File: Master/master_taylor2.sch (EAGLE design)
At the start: 43 parts, among them J1 ISP, U1 ATMEGA128RFA1, U2 TPS73633-DBVT, U3 ULN2003ADR, Y1 16MHz

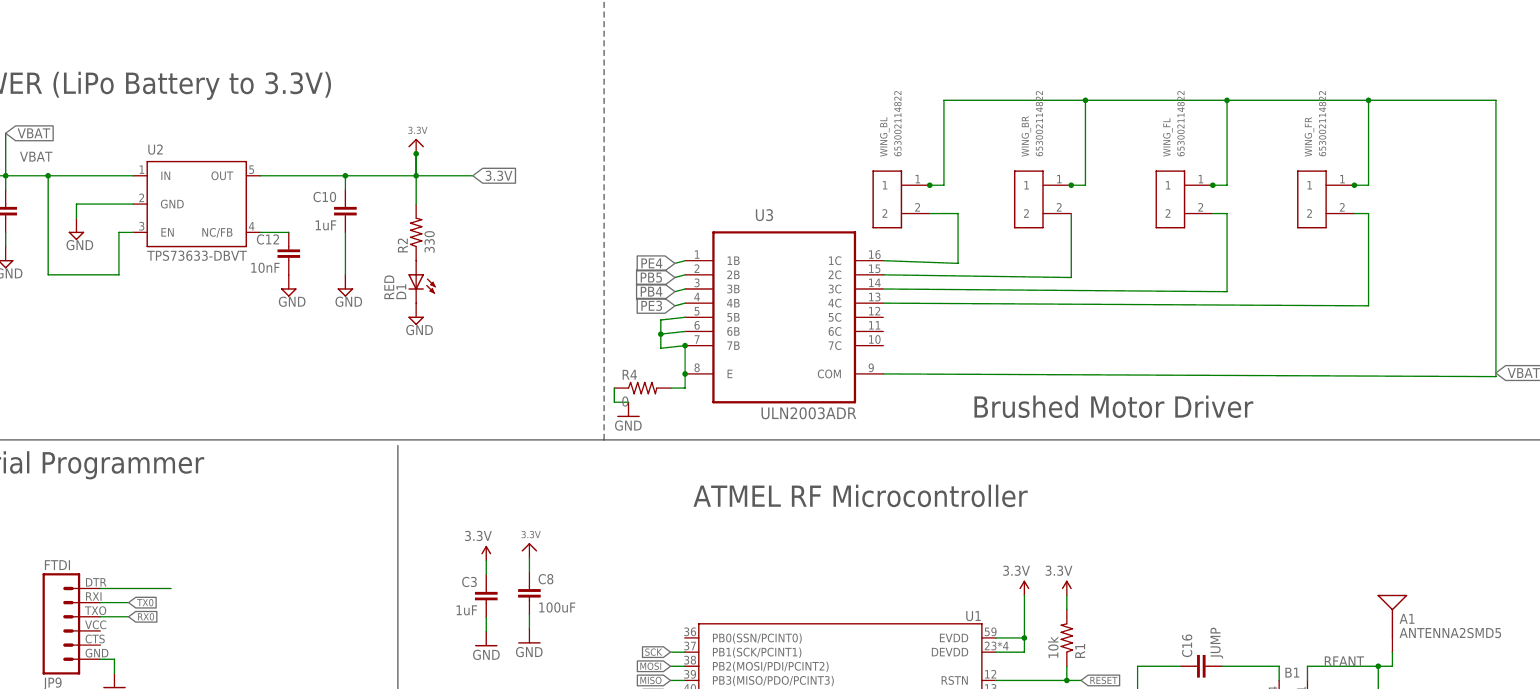
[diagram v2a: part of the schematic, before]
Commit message: Added caps near each motor
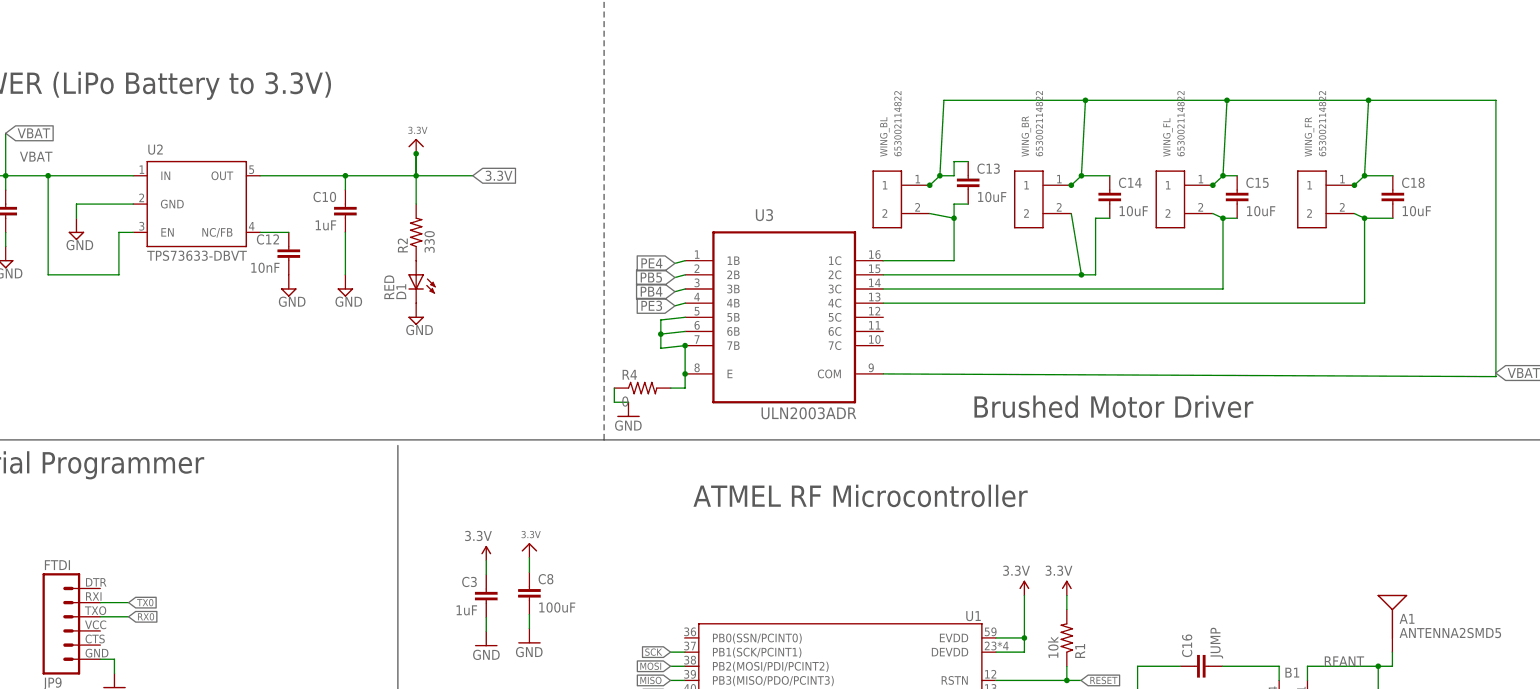
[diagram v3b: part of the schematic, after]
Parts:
- added C13, C14, C15, C18: 10uF, SparkFun-Capacitors:CAP0603-CAP
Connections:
- removed net DTR: JP9.1
- net N$29: now also C13.2
- net N$30: now also C14.2
- net N$31: now also C15.2
- net N$32: now also C18.2
- net VBAT: now also C13.1, C14.1, C15.1, C18.1
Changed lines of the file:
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@@
 <setting verticaltext="up"/>
 </settings>
-<grid distance="0.1" unitdist="inch" unit="inch" style="lines" multiple="1" display="no" altdistance="0.01" altunitdist="inch" altunit="inch"/>
+<grid distance="0.1" unitdist="inch" unit="inch" style="lines" multiple="1" display="yes" altdistance="0.01" altunitdist="inch" altunit="inch"/>
 <layers>
 <layer number="1" name="Top" color="4" fill="1" visible="no" active="no"/>
@@
 <part name="U$8" library="microbuilder" deviceset="3.3V" device=""/>
 <part name="GND8" library="SparkFun-Aesthetics" deviceset="GND" device=""/>
+<part name="C13" library="SparkFun-Capacitors" deviceset="CAP" device="0603-CAP" value="10uF"/>
+<part name="C14" library="SparkFun-Capacitors" deviceset="CAP" device="0603-CAP" value="10uF"/>
+<part name="C15" library="SparkFun-Capacitors" deviceset="CAP" device="0603-CAP" value="10uF"/>
+<part name="C18" library="SparkFun-Capacitors" deviceset="CAP" device="0603-CAP" value="10uF"/>
 </parts>
 <sheets>
@@
 <instance part="U$8" gate="G$1" x="-152.4" y="213.36"/>
 <instance part="GND8" gate="1" x="-152.4" y="195.58"/>
+<instance part="C13" gate="G$1" x="-73.66" y="276.86"/>
+<instance part="C14" gate="G$1" x="-48.26" y="274.32"/>
+<instance part="C15" gate="G$1" x="-25.4" y="274.32"/>
+<instance part="C18" gate="G$1" x="2.54" y="274.32"/>
 </instances>
 <busses>
@@
 </segment>
 </net>
-<net name="DTR" class="0">
-<segment>
-<pinref part="JP9" gate="G$1" pin="1"/>
-<wire x1="-216.7" y1="205.34" x2="-229.4" y2="205.34" width="0.1524" layer="91"/>
-</segment>
-</net>
 <net name="N$7" class="0">
 <segment>
@@
 <segment>
 <pinref part="U3" gate="A" pin="1C"/>
-<wire x1="-88.9" y1="264.16" x2="-75.48" y2="263.68" width="0.1524" layer="91"/>
-<wire x1="-75.48" y1="263.68" x2="-75.48" y2="272.62" width="0.1524" layer="91"/>
+<wire x1="-88.9" y1="264.16" x2="-76.2" y2="264.16" width="0.1524" layer="91"/>
+<wire x1="-76.2" y1="264.16" x2="-76.2" y2="271.78" width="0.1524" layer="91"/>
 <pinref part="WING_BL" gate="G$1" pin="2"/>
-<wire x1="-75.48" y1="272.62" x2="-80.56" y2="272.62" width="0.1524" layer="91"/>
+<wire x1="-76.2" y1="271.78" x2="-80.56" y2="272.62" width="0.1524" layer="91"/>
+<wire x1="-73.66" y1="274.32" x2="-76.2" y2="274.32" width="0.1524" layer="91"/>
+<wire x1="-76.2" y1="274.32" x2="-76.2" y2="271.78" width="0.1524" layer="91"/>
+<junction x="-76.2" y="271.78"/>
+<pinref part="C13" gate="G$1" pin="2"/>
 </segment>
 </net>
@@
 <pinref part="U3" gate="A" pin="2C"/>
 <pinref part="WING_BR" gate="G$1" pin="2"/>
-<wire x1="-88.9" y1="261.62" x2="-55.16" y2="261.14" width="0.1524" layer="91"/>
-<wire x1="-55.16" y1="261.14" x2="-55.16" y2="272.62" width="0.1524" layer="91"/>
+<wire x1="-88.9" y1="261.62" x2="-53.34" y2="261.62" width="0.1524" layer="91"/>
+<wire x1="-53.34" y1="261.62" x2="-55.16" y2="272.62" width="0.1524" layer="91"/>
+<wire x1="-48.26" y1="271.78" x2="-50.8" y2="271.78" width="0.1524" layer="91"/>
+<wire x1="-50.8" y1="271.78" x2="-50.8" y2="261.62" width="0.1524" layer="91"/>
+<wire x1="-50.8" y1="261.62" x2="-53.34" y2="261.62" width="0.1524" layer="91"/>
+<junction x="-53.34" y="261.62"/>
+<pinref part="C14" gate="G$1" pin="2"/>
 </segment>
 </net>
@@
 <segment>
 <pinref part="U3" gate="A" pin="3C"/>
-<wire x1="-88.9" y1="259.08" x2="-27.22" y2="258.6" width="0.1524" layer="91"/>
-<wire x1="-27.22" y1="258.6" x2="-27.22" y2="272.62" width="0.1524" layer="91"/>
+<wire x1="-88.9" y1="259.08" x2="-27.94" y2="259.08" width="0.1524" layer="91"/>
+<wire x1="-27.94" y1="259.08" x2="-27.94" y2="271.78" width="0.1524" layer="91"/>
 <pinref part="WING_FL" gate="G$1" pin="2"/>
-<wire x1="-27.22" y1="272.62" x2="-29.76" y2="272.62" width="0.1524" layer="91"/>
+<wire x1="-27.94" y1="271.78" x2="-29.76" y2="272.62" width="0.1524" layer="91"/>
+<wire x1="-27.94" y1="271.78" x2="-25.4" y2="271.78" width="0.1524" layer="91"/>
+<junction x="-27.94" y="271.78"/>
+<pinref part="C15" gate="G$1" pin="2"/>
 </segment>
 </net>
@@
 <segment>
 <pinref part="U3" gate="A" pin="4C"/>
-<wire x1="-88.9" y1="256.54" x2="-1.82" y2="256.06" width="0.1524" layer="91"/>
-<wire x1="-1.82" y1="256.06" x2="-1.82" y2="272.62" width="0.1524" layer="91"/>
+<wire x1="-88.9" y1="256.54" x2="-2.54" y2="256.54" width="0.1524" layer="91"/>
+<wire x1="-2.54" y1="256.54" x2="-2.54" y2="271.78" width="0.1524" layer="91"/>
 <pinref part="WING_FR" gate="G$1" pin="2"/>
-<wire x1="-1.82" y1="272.62" x2="-4.36" y2="272.62" width="0.1524" layer="91"/>
+<wire x1="-2.54" y1="271.78" x2="-4.36" y2="272.62" width="0.1524" layer="91"/>
+<wire x1="-2.54" y1="271.78" x2="2.54" y2="271.78" width="0.1524" layer="91"/>
+<junction x="-2.54" y="271.78"/>
+<pinref part="C18" gate="G$1" pin="2"/>
 </segment>
 </net>
@@
 <wire x1="-27.22" y1="292.94" x2="-52.62" y2="292.94" width="0.1524" layer="91"/>
 <wire x1="-52.62" y1="292.94" x2="-78.02" y2="292.94" width="0.1524" layer="91"/>
-<wire x1="-78.02" y1="292.94" x2="-78.02" y2="277.7" width="0.1524" layer="91"/>
+<wire x1="-78.02" y1="292.94" x2="-78.74" y2="279.4" width="0.1524" layer="91"/>
 <pinref part="WING_BL" gate="G$1" pin="1"/>
-<wire x1="-78.02" y1="277.7" x2="-80.56" y2="277.7" width="0.1524" layer="91"/>
+<wire x1="-78.74" y1="279.4" x2="-80.56" y2="277.7" width="0.1524" layer="91"/>
 <pinref part="WING_BR" gate="G$1" pin="1"/>
-<wire x1="-55.16" y1="277.7" x2="-52.62" y2="277.7" width="0.1524" layer="91"/>
-<wire x1="-52.62" y1="277.7" x2="-52.62" y2="292.94" width="0.1524" layer="91"/>
+<wire x1="-55.16" y1="277.7" x2="-53.34" y2="279.4" width="0.1524" layer="91"/>
+<wire x1="-53.34" y1="279.4" x2="-52.62" y2="292.94" width="0.1524" layer="91"/>
 <pinref part="WING_FL" gate="G$1" pin="1"/>
-<wire x1="-29.76" y1="277.7" x2="-27.22" y2="277.7" width="0.1524" layer="91"/>
-<wire x1="-27.22" y1="277.7" x2="-27.22" y2="292.94" width="0.1524" layer="91"/>
-<wire x1="-1.82" y1="277.7" x2="-1.82" y2="292.94" width="0.1524" layer="91"/>
+<wire x1="-29.76" y1="277.7" x2="-27.94" y2="279.4" width="0.1524" layer="91"/>
+<wire x1="-27.94" y1="279.4" x2="-27.22" y2="292.94" width="0.1524" layer="91"/>
+<wire x1="-2.54" y1="279.4" x2="-1.82" y2="292.94" width="0.1524" layer="91"/>
 <pinref part="WING_FR" gate="G$1" pin="1"/>
-<wire x1="-4.36" y1="277.7" x2="-1.82" y2="277.7" width="0.1524" layer="91"/>
+<wire x1="-4.36" y1="277.7" x2="-2.54" y2="279.4" width="0.1524" layer="91"/>
 <junction x="-27.22" y="292.94"/>
 <junction x="-52.62" y="292.94"/>
@@
 <junction x="-4.36" y="277.7"/>
 <label x="21" y="244" size="1.778" layer="97" xref="yes"/>
-</segment>
-</net>
+<wire x1="-78.74" y1="279.4" x2="-76.2" y2="279.4" width="0.1524" layer="91"/>
+<wire x1="-76.2" y1="279.4" x2="-76.2" y2="281.94" width="0.1524" layer="91"/>
+<wire x1="-76.2" y1="281.94" x2="-73.66" y2="281.94" width="0.1524" layer="91"/>
+<wire x1="-27.94" y1="279.4" x2="-25.4" y2="279.4" width="0.1524" layer="91"/>
+<wire x1="-2.54" y1="279.4" x2="2.54" y2="279.4" width="0.1524" layer="91"/>
+<wire x1="-53.34" y1="279.4" x2="-48.26" y2="279.4" width="0.1524" layer="91"/>
+<junction x="-53.34" y="279.4"/>
+<junction x="-27.94" y="279.4"/>
+<junction x="-2.54" y="279.4"/>
+<junction x="-78.74" y="279.4"/>
+<pinref part="C13" gate="G$1" pin="1"/>
+<pinref part="C14" gate="G$1" pin="1"/>
+<pinref part="C15" gate="G$1" pin="1"/>
+<pinref part="C18" gate="G$1" pin="1"/>
+</segment>
+</net>

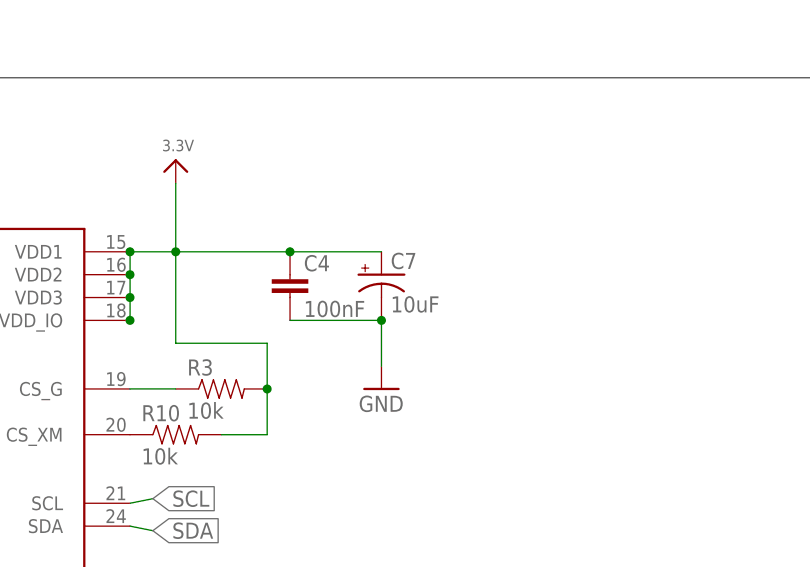
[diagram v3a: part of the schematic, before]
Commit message: Sparkfun's electrolytic footprint seemed sketchy so I switched to microbuilder
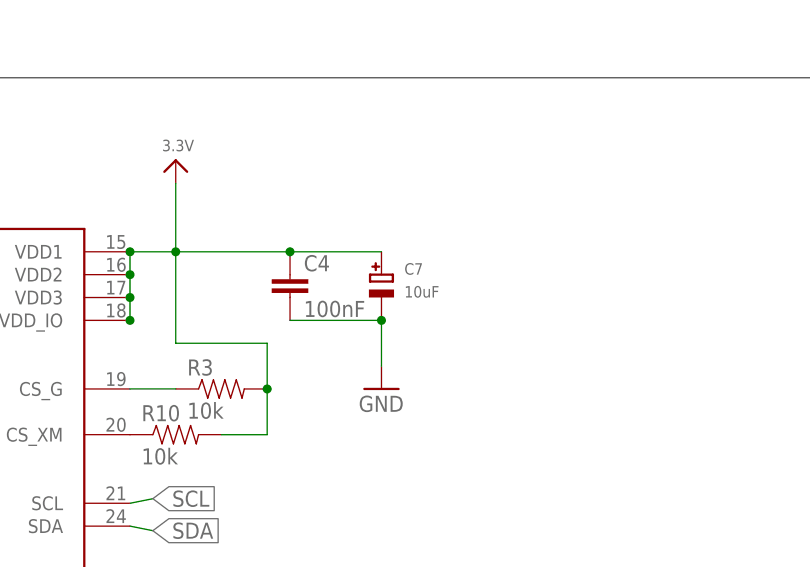
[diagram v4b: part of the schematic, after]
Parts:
- C7: device SparkFun-Capacitors:10UF-20V-10%(TANT) -> microbuilder:CAP_TANTALUMA/3216_WAVE
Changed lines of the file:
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@@
 <part name="R10" library="SparkFun-Passives" deviceset="RESISTOR" device="0805-RES" value="10k"/>
 <part name="R4" library="SparkFun-Passives" deviceset="RESISTOR" device="0805-RES" value="0"/>
-<part name="C7" library="SparkFun-Capacitors" deviceset="10UF-20V-10%(TANT)" device="" value="10uF"/>
+<part name="C7" library="microbuilder" deviceset="CAP_TANTALUM" device="A/3216_WAVE" value="10uF"/>
 <part name="C8" library="SparkFun-Capacitors" deviceset="CAP" device="1206" value="100uF"/>
 <part name="U$8" library="microbuilder" deviceset="3.3V" device=""/>
@@
 <instance part="R10" gate="G$1" x="-149.86" y="53.34"/>
 <instance part="R4" gate="G$1" x="-132.08" y="241.3"/>
-<instance part="C7" gate="G$1" x="-127" y="71.12"/>
+<instance part="C7" gate="G$1" x="-127" y="68.58"/>
 <instance part="C8" gate="G$1" x="-152.4" y="203.2"/>
 <instance part="U$8" gate="G$1" x="-152.4" y="213.36"/>
